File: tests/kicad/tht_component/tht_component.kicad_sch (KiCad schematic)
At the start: 5 parts, among them J1 VIN, J2 VOUT, J3 VOUT

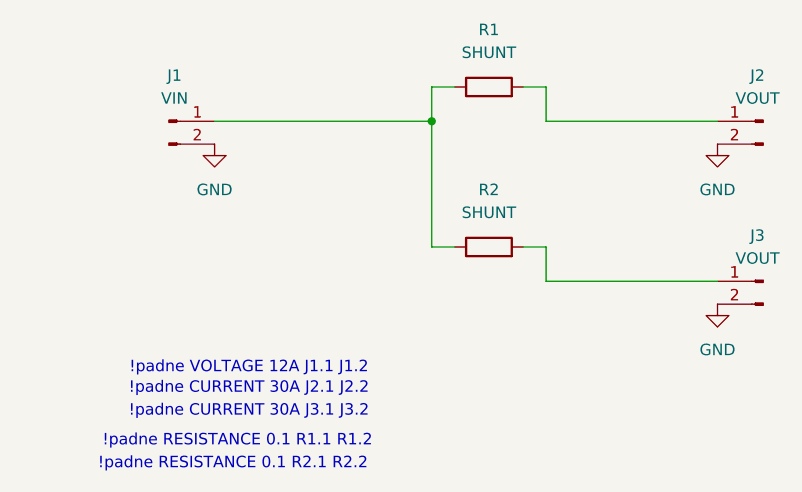
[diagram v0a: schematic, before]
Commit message: feat: Richer directive syntax
This commit adds support for named directive parameters. No more
guessing which parameter is the positive terminal positive and which is the
negative terminal!
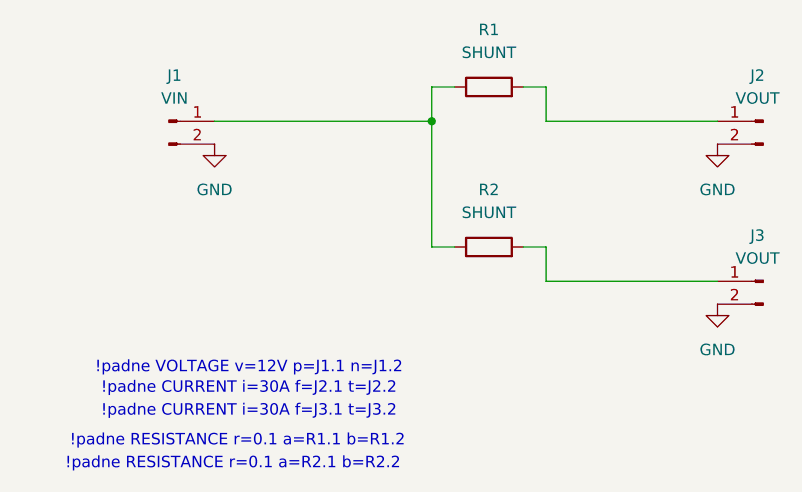
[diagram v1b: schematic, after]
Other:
- note added: "!padne CURRENT i=30A f=J2.1 t=J2.2"
- note added: "!padne CURRENT i=30A f=J3.1 t=J3.2"
- note added: "!padne RESISTANCE r=0.1 a=R1.1 b=R1.2"
- note added: "!padne RESISTANCE r=0.1 a=R2.1 b=R2.2"
- note added: "!padne VOLTAGE v=12V p=J1.1 n=J1.2"
- note removed: "!padne CURRENT 30A J2.1 J2.2"
- note removed: "!padne CURRENT 30A J3.1 J3.2"
- note removed: "!padne RESISTANCE 0.1 R1.1 R1.2"
- note removed: "!padne RESISTANCE 0.1 R2.1 R2.2"
- note removed: "!padne VOLTAGE 12A J1.1 J1.2"
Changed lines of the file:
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@@
 		)
 	)
-	(text "!padne CURRENT 30A J3.1 J3.2"
+	(text "!padne CURRENT i=30A f=J3.1 t=J3.2"
 		(exclude_from_sim no)
 		(at 90.17 142.748 0)
@@
 		)
 	)
-	(text "!padne RESISTANCE 0.1 R1.1 R1.2"
+	(text "!padne RESISTANCE r=0.1 a=R1.1 b=R1.2"
 		(exclude_from_sim no)
 		(at 88.9 146.05 0)
@@
 		)
 	)
-	(text "!padne RESISTANCE 0.1 R2.1 R2.2"
+	(text "!padne RESISTANCE r=0.1 a=R2.1 b=R2.2"
 		(exclude_from_sim no)
 		(at 88.392 148.59 0)
@@
 		)
 	)
-	(text "!padne VOLTAGE 12A J1.1 J1.2"
+	(text "!padne VOLTAGE v=12V p=J1.1 n=J1.2"
 		(exclude_from_sim no)
 		(at 90.17 137.922 0)
@@
 		)
 	)
-	(text "!padne CURRENT 30A J2.1 J2.2"
+	(text "!padne CURRENT i=30A f=J2.1 t=J2.2"
 		(exclude_from_sim no)
 		(at 90.17 140.208 0)
